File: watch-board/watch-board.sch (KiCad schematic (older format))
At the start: 32 parts

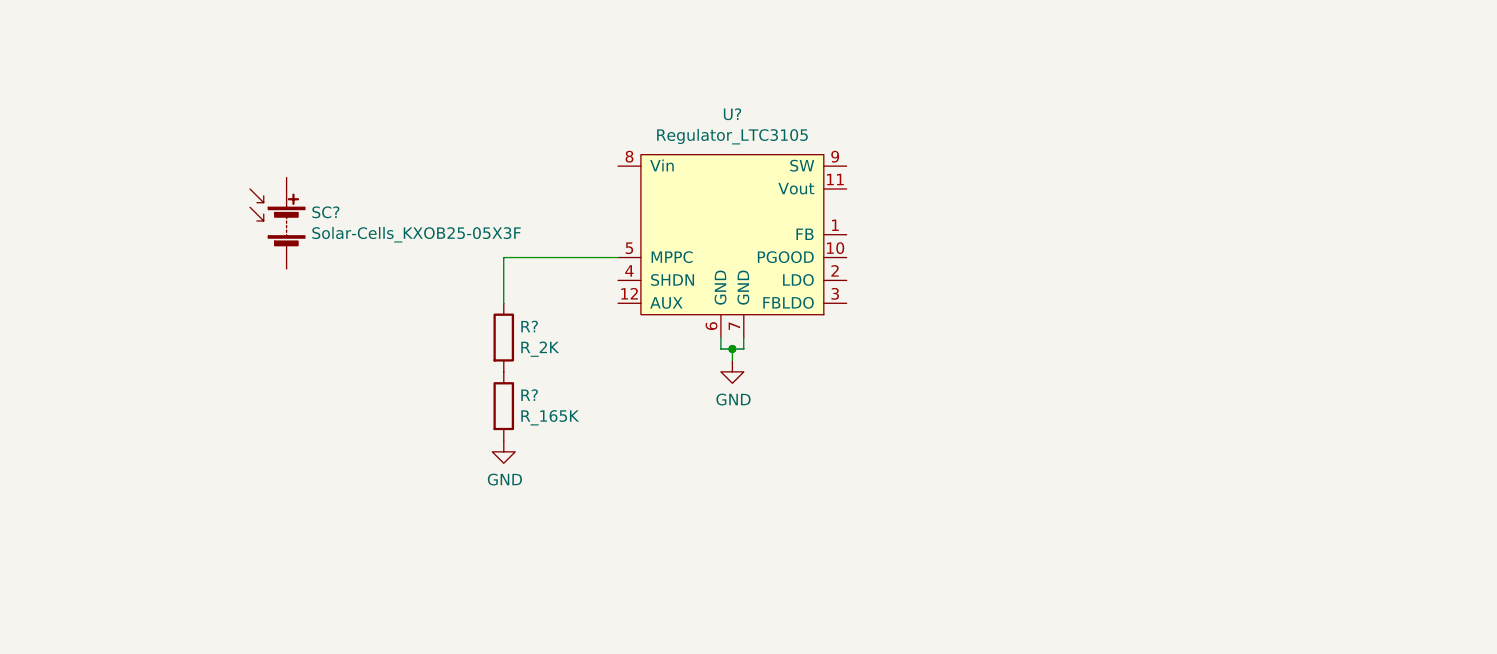
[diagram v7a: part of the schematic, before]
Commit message: switching to BQ25570 & LTC3531 combo
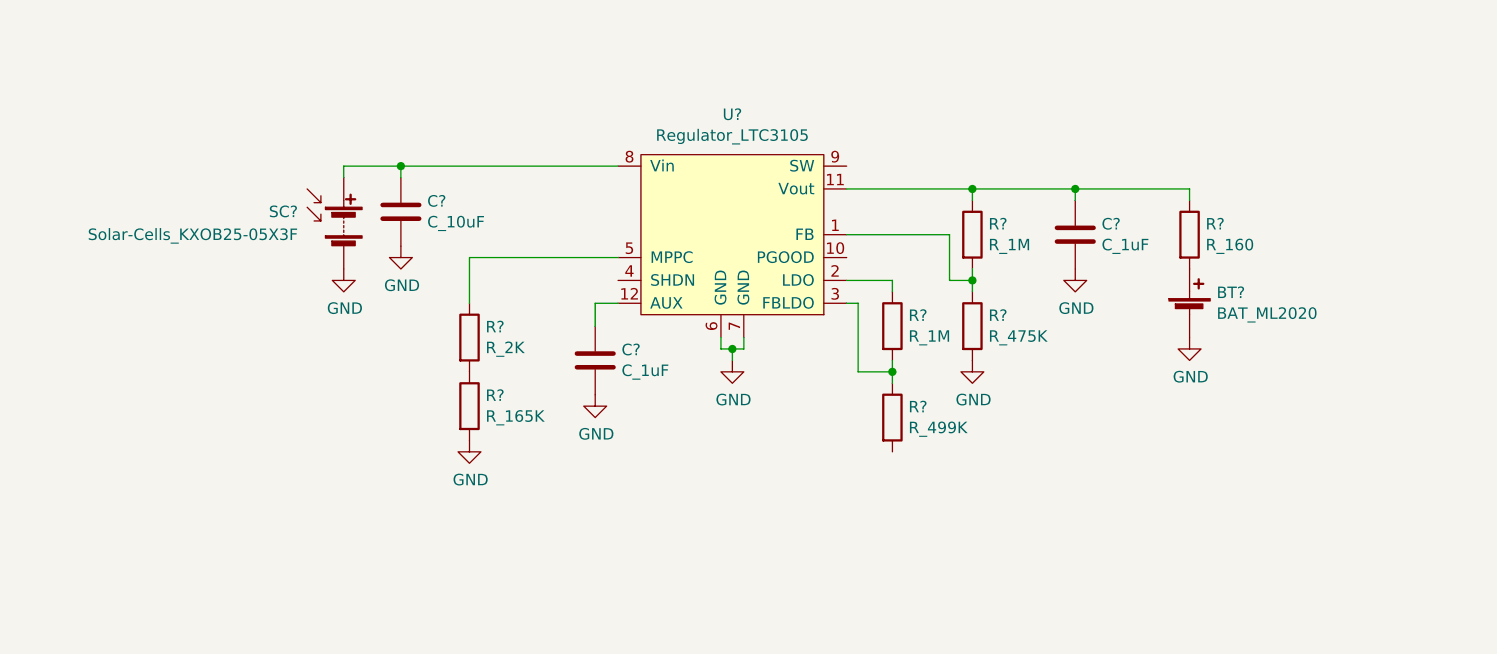
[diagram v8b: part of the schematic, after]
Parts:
- added BT?: BAT_ML2020, symbol luke:BAT_ML2020
- added C?: C_10uF, Capacitor_SMD:C_0805_2012Metric, symbol luke:C_10uF
- added C? (x2): C_1uF, footprints:C_0805_OEM, symbol formula:C_1uF
- added R? (x2): R_1M, Resistor_SMD:R_0805_2012Metric, symbol luke:R_1M
- added R?: R_475K, Resistor_SMD:R_0805_2012Metric, symbol luke:R_475K
- added R?: R_499K, Resistor_SMD:R_0805_2012Metric, symbol luke:R_499K
- added R?: R_160, Resistor_SMD:R_0805_2012Metric, symbol luke:R_160
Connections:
- net GND: now also SC?.2 (-), BT?.2 (-), C?.2, C?.2, C?.2, R?.2
- net at U?.1 (FB): now also R?.1, R?.2
- net at U?.11 (Vout): now also C?.1, R?.1, R?.1
- net at U?.12 (AUX): now also C?.1
- net at U?.2 (LDO): now also R?.1
- net at U?.3 (FBLDO): now also R?.1, R?.2
- net at U?.8 (Vin): now also SC?.1 (+), C?.1
- new net: BT?.1 (+), R?.2
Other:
- moved on the sheet: R?, SC?
